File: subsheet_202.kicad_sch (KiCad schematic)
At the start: 6 parts, among them J1101 Parallel and Serial breakout, J203 DB-25S Parallel port, U202 YM2149_PHY

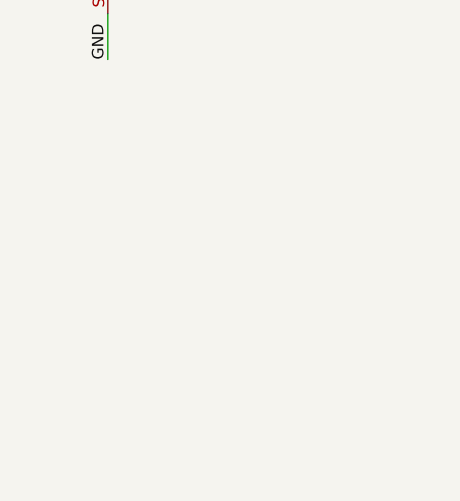
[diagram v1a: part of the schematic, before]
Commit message: add gnd/vcc symbol to start replacing local labels
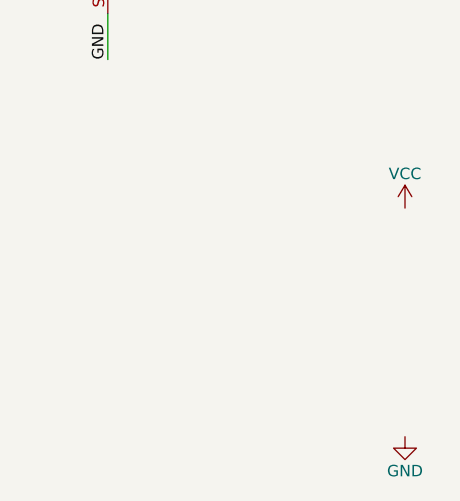
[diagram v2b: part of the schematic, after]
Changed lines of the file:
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@@
     (pin "9")
   )
+  (symbol (lib_id "power:VCC") (at 184.15 217.17 0) (unit 1)
+    (in_bom yes) (on_board yes)
+    (property "Reference" "#PWR?" (id 0) (at 184.15 220.98 0)
+      (effects (font (size 1.27 1.27)) hide)
+    )
+    (property "Value" "VCC" (id 1) (at 184.15 213.36 0))
+    (property "Footprint" "" (id 2) (at 184.15 217.17 0)
+      (effects (font (size 1.27 1.27)) hide)
+    )
+    (property "Datasheet" "" (id 3) (at 184.15 217.17 0)
+      (effects (font (size 1.27 1.27)) hide)
+    )
+    (pin "1")
+  )
+  (symbol (lib_id "power:GND") (at 184.15 242.57 0) (unit 1)
+    (in_bom yes) (on_board yes)
+    (property "Reference" "#PWR?" (id 0) (at 184.15 248.92 0)
+      (effects (font (size 1.27 1.27)) hide)
+    )
+    (property "Value" "GND" (id 1) (at 184.15 246.38 0))
+    (property "Footprint" "" (id 2) (at 184.15 242.57 0)
+      (effects (font (size 1.27 1.27)) hide)
+    )
+    (property "Datasheet" "" (id 3) (at 184.15 242.57 0)
+      (effects (font (size 1.27 1.27)) hide)
+    )
+    (pin "1")
+  )
 )
